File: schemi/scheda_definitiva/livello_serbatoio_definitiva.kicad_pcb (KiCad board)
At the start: 2 copper layers, 83 x 72 mm, 36 parts, among them J1 USB_B, J2 CONN_US, J3 CONN_LCD, J4 BTN_LED_GROUP, J5 Conn_01x06_Male, SW1 SW_RST, U1 FT232RL, U2 ATmega328P-PU, Y1 16MHz

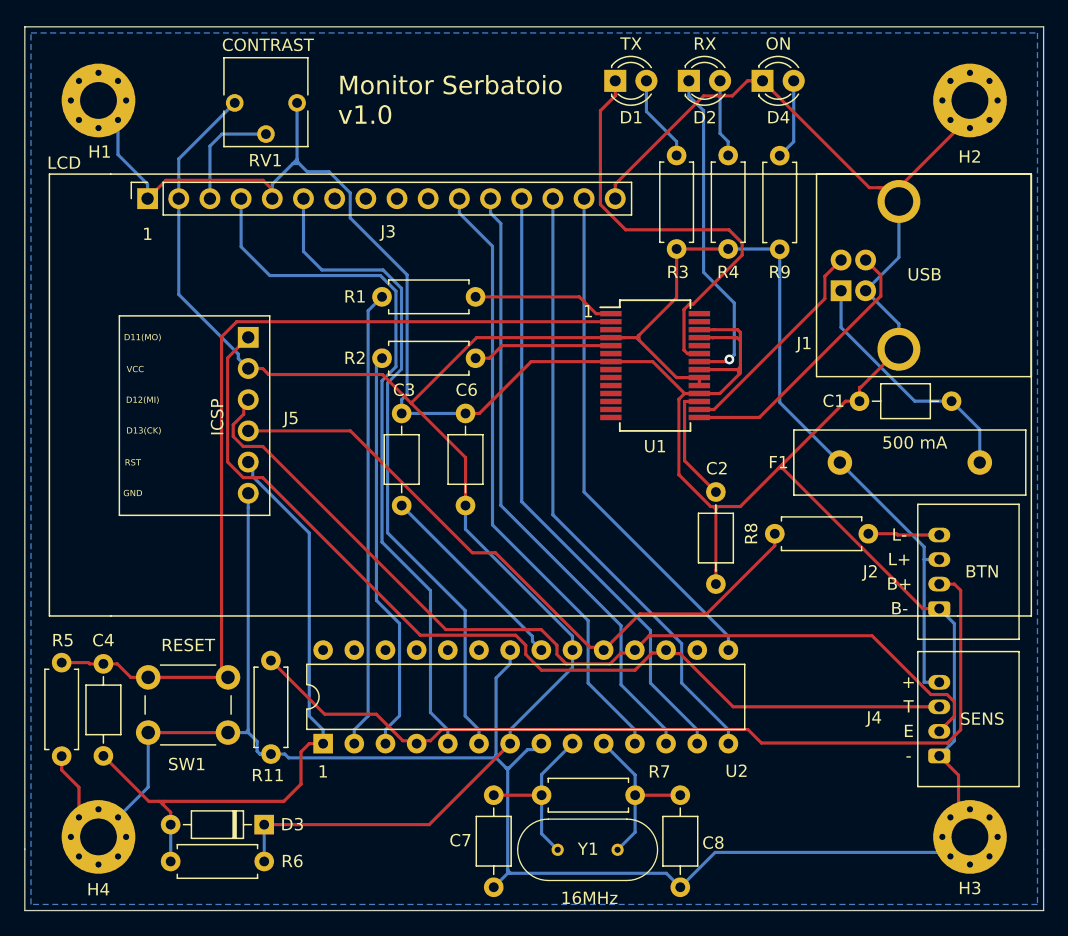
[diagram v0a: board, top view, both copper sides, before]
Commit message: fix alimentazioni + introduzione coppia differenziale per USB - da rivedere piste USB per match lunghezza/skew/impedenza
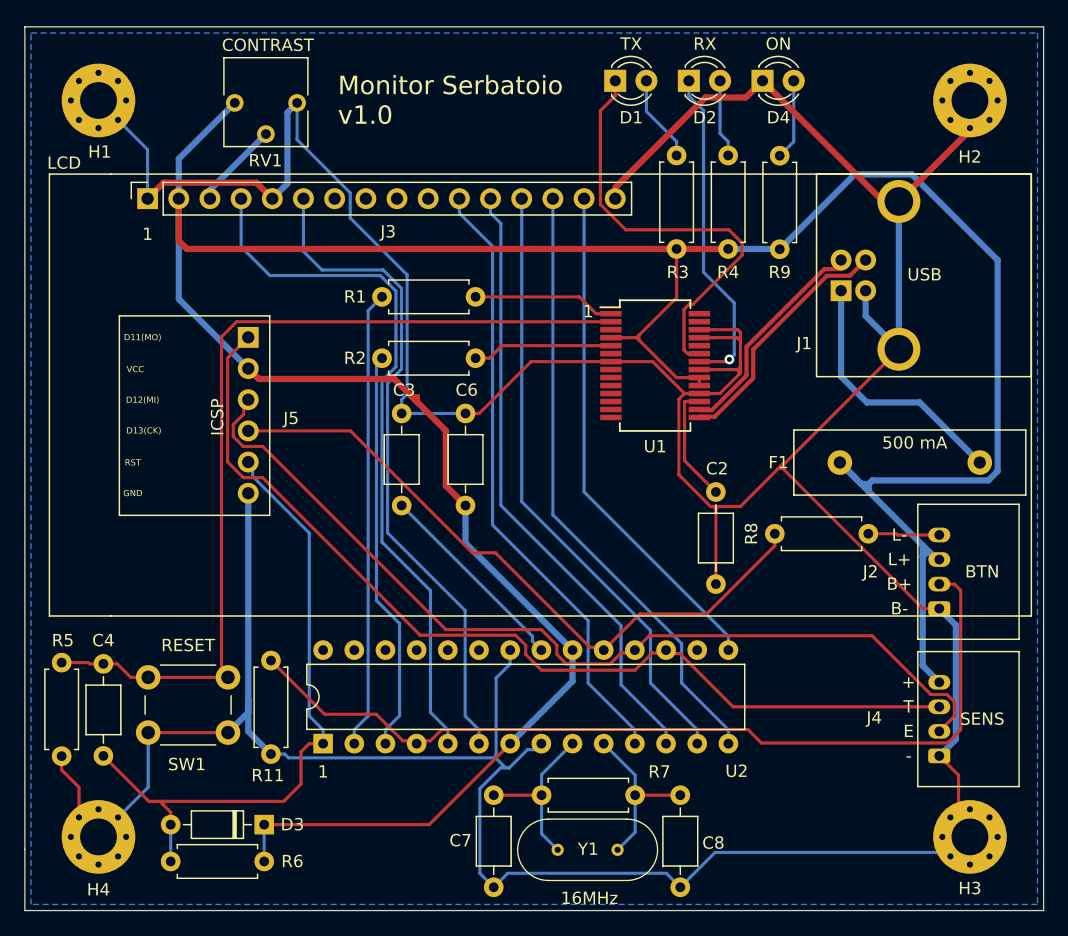
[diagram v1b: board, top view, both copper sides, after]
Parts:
- removed C1: 100nF, Capacitor_THT:C_Axial_L3.8mm_D2.6mm_P7.50mm_Horizontal
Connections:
- net Net-(J1-Pad2) renamed /D-
- net Net-(J1-Pad3) renamed /D+
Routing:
- net VDD: track 190.3 -> 266.2 mm
- net BLK: track 414.0 -> 431.4 mm
- net V0: track 9.25 -> 7.15 mm
- net /D+: track 22.3 -> 20.5 mm
- net /D-: track 17.7 -> 19.1 mm
- net Net-(C1-Pad1): track 20.4 -> 21.2 mm

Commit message: spostati componenti e fatto nuovo sbroglio
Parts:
- removed F1: 500mA, Fuse:Fuse_Littelfuse-LVR100
- added C1: 100nF, Capacitor_THT:C_Radial_D5.0mm_H5.0mm_P2.00mm, F.Cu at (155.6, 102.8)
- added FB1: MF-MSMF050-2, Inductor_SMD:L_1812_4532Metric_Pad1.30x3.40mm_HandSolder, F.Cu at (149.7, 105.1)
- C2, C3, C4, C6, C7, C8: footprint Capacitor_THT:C_Axial_L3.8mm_D2.6mm_P7.50mm_Horizontal -> Capacitor_THT:C_Radial_D5.0mm_H5.0mm_P2.00mm
- J1: footprint Connector_USB:USB_B_OST_USB-B1HSxx_Horizontal -> simboli_custom:USB_B_OST_USB-B1HSxx_Horizontal
- J5: value Conn_01x06_Male -> ICSP; footprint Connector_PinHeader_2.54mm:PinHeader_1x06_P2.54mm_Horizontal -> Connector_PinHeader_2.54mm:PinHeader_2x03_P2.54mm_Vertical; moved to F.Cu
- U1: moved to B.Cu
- moved J5 63.0 mm to (155.0, 131.9), turned to 270 degrees
- moved R11 51.3 mm to (157.9, 125.9), turned to 180 degrees
- moved C2 16.7 mm to (154.2, 93.3)
- moved C6 12.7 mm to (134.0, 113.2), turned to 180 degrees
- moved R8 12.4 mm to (150.3, 121.5)
- moved J4 12.1 mm to (162.3, 127.5)
- moved C3 12.1 mm to (128.2, 113.1), turned to 180 degrees
- moved R1 11.4 mm to (125.0, 97.2)
- moved J2 11.4 mm to (162.3, 116.1)
- moved J1 9.83 mm to (160.8, 96.1)
- moved R2 8.93 mm to (125.0, 93.9)
- moved R5 5.41 mm to (92.3, 114.9)
- moved U1 5.13 mm to (143.2, 94.0)
- moved C8 3.76 mm to (141.6, 134.5)
- moved C7 3.73 mm to (124.1, 134.5)
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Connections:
- net Net-(C7-Pad2) renamed /X1
- net Net-(C8-Pad2) renamed /X2
- J5 pad 1: D11 -> D12
- J5 pad 3: D12 -> D13
- J5 pad 4: D13 -> D11
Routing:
- net TX: track 37.3 -> 77.4 mm
- net RX: track 32.8 -> 71.5 mm
- net ICSP_RST: track 54.0 -> 80.7 mm, vias 0 -> 1
- net D13: track 54.8 -> 30.8 mm
- net D2: track 73.7 -> 91.6 mm, vias 0 -> 2
- net DTR: track 74.0 -> 91.9 mm, vias 0 -> 1
- net D12: track 76.5 -> 62.9 mm
- net D11: track 78.9 -> 66.2 mm
- net Net-(C3-Pad1): track 16.5 -> 6.09 mm
- net BLA: track 41.7 -> 50.5 mm
- net VDD: track 266.2 -> 257.9 mm, vias 0 -> 1
- net D8: track 50.3 -> 56.7 mm
- net D3: track 57.6 -> 51.6 mm
- net Net-(C1-Pad1): track 21.2 -> 15.3 mm
- net D5: track 50.3 -> 55.0 mm
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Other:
- net class USB added: clearance 0.0508, trace_width 0.254, via_dia 0.8, via_drill 0.4
- board text added: "+5V"
- board text added: "ECHO"
- board text added: "MISO"
- board text added: "MOSI"
- board text added: "SCK"
- board text added: "TRIG"
- board text removed: "500 mA"
- board text removed: "D11(MO)"
- board text removed: "D12(MI)"
- board text removed: "D13(CK)"
- board text removed: "E"
- board text removed: "ICSP"
- board text removed: "J1"
- board text removed: "J2"
- board text removed: "J4"
- board text removed: "J5"
- board text removed: "T"
- board text removed: "USB"
- board text removed: "VCC"

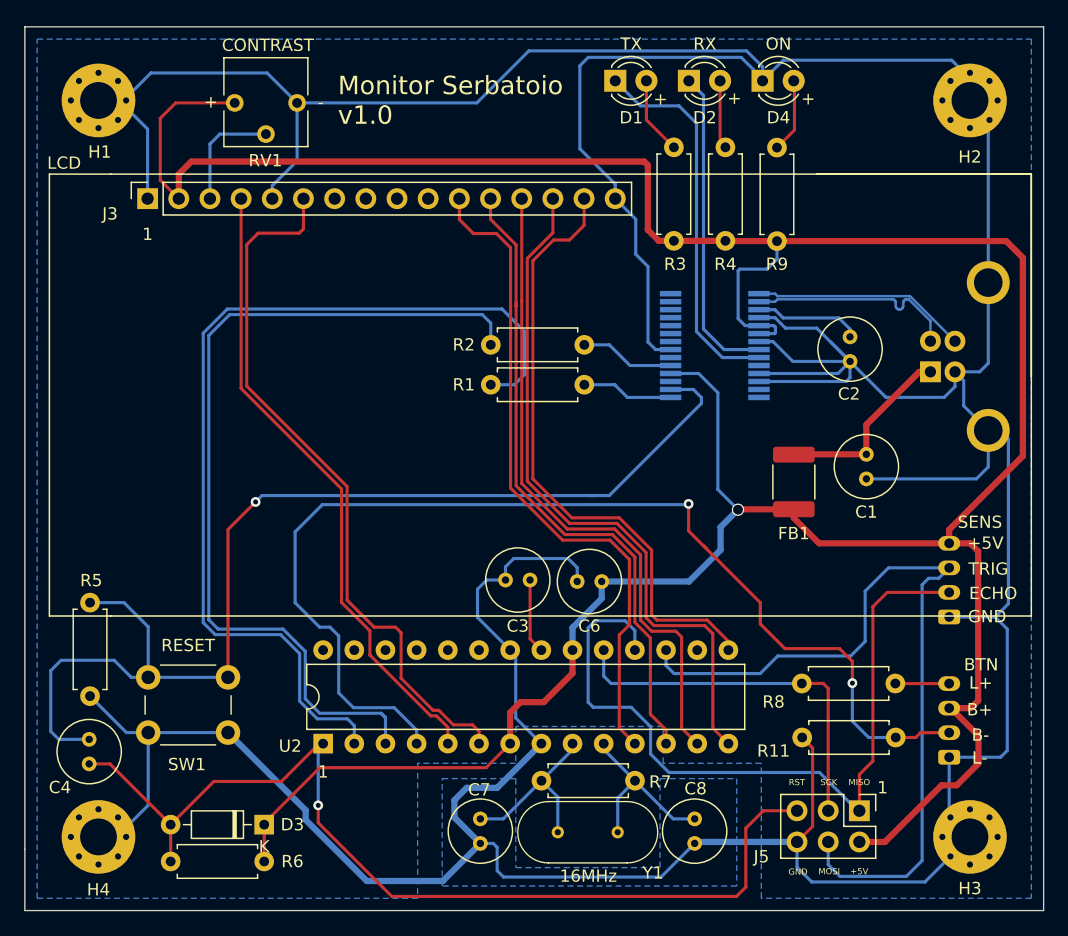
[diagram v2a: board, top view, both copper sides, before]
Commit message: rivisto routing di alcune piste
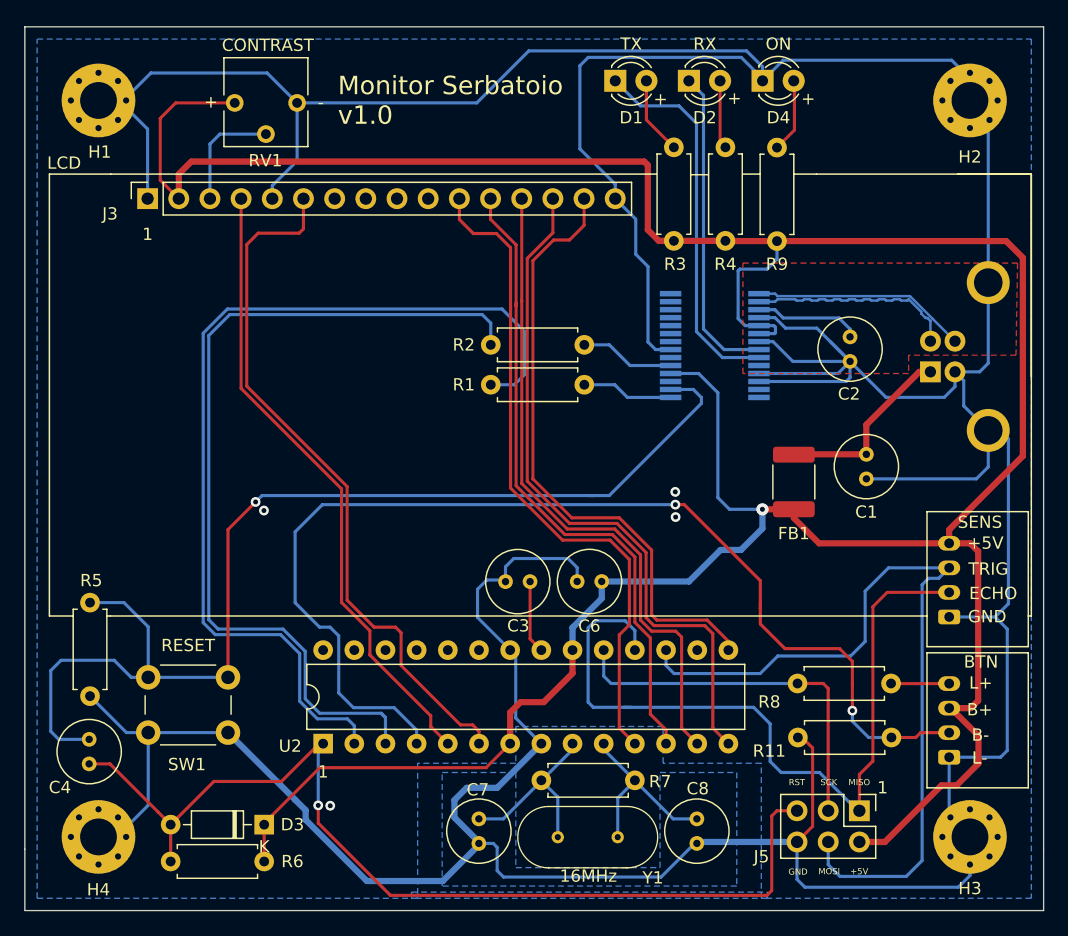
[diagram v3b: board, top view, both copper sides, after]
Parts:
- moved Y1 0.40 mm to (132.9, 134.0)
- moved R8 0.35 mm to (149.9, 121.5)
- moved R11 0.35 mm to (157.6, 125.9)
- moved C8 0.18 mm to (141.8, 134.5)
- moved C3 0.13 mm to (128.2, 113.2)
- moved C7 0.12 mm to (124.0, 134.5)
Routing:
- net BLK: track 432.0 -> 427.0 mm, vias 0 -> 4
- net VDD: track 257.9 -> 260.1 mm
- net D12: track 62.9 -> 64.0 mm
- net ICSP_RST: track 80.7 -> 81.3 mm
- net D4: track 58.3 -> 57.7 mm
- added copper zone on F.Cu, net BLK

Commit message: modifica traccia usb + rigenerato gerber
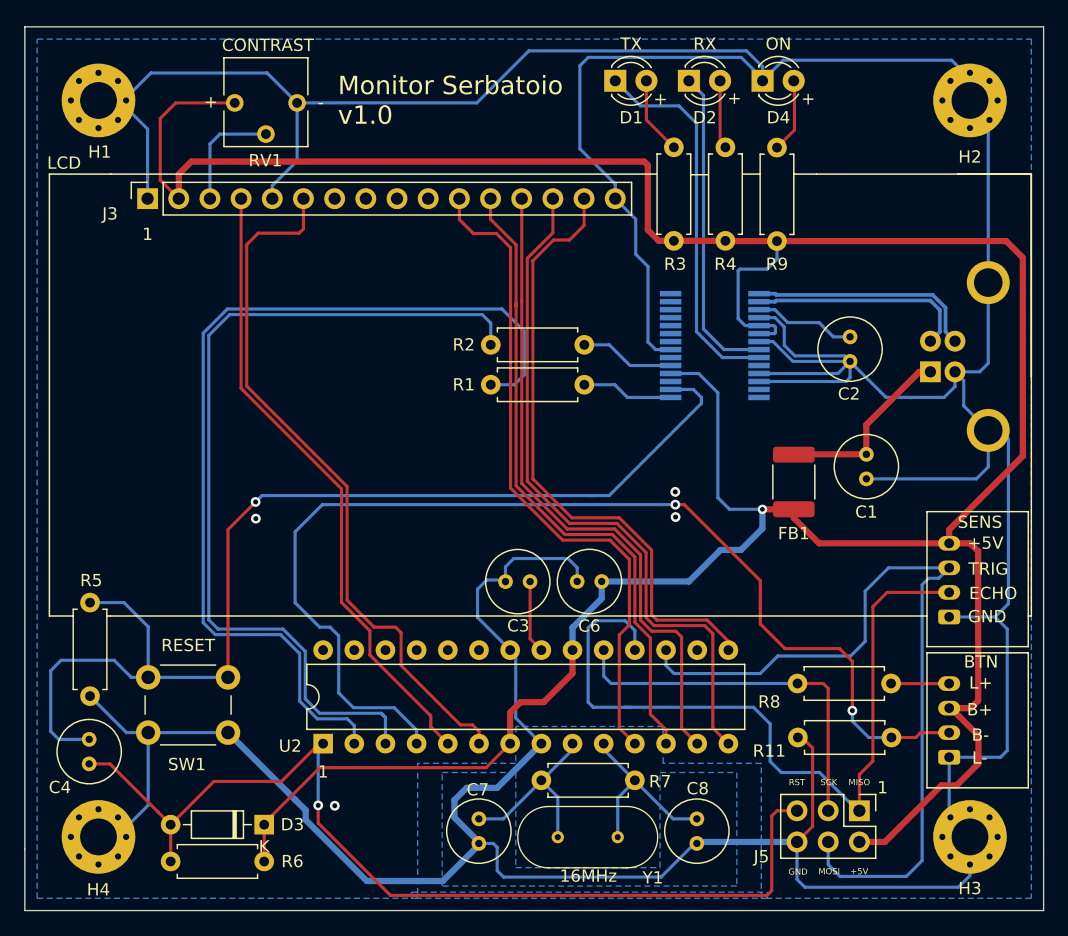
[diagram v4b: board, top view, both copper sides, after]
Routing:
- net BLK: track 427.0 -> 425.6 mm
- net /D+: track 17.6 -> 18.7 mm
- net /D-: track 17.2 -> 18.0 mm
- removed copper zone on F.Cu, net BLK
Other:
- net class USB: clearance 0.0508 -> 0.15
- rule pad_to_mask_clearance: 0.05 -> 0

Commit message: modificato gerber / disegno 3D box / nuove immagini render aggiunte
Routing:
- net BLK: vias 4 -> 6
